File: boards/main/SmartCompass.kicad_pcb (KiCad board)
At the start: 4 copper layers, 70 x 70 mm, 124 parts, among them IC1 Wio-SX1262, J1 SWD HEADER, J2 EXPANSION, J3 FH12A-24S-0.5SH(55), J5 IPEX, P1 JST_BTN_1, P2 JST_BTN_2, P3 JST_BTN_3, Q1 DMG3415U, Q2 Si1308EDL, U1 BMD-340-A-R, U2 MX25R6435FZAIH0, U3 RT9080-33GJ5, U4 MCP73831T-2ACI_OT, U5 MAX17048G_T10, U6 BNO085, U7 DRV2605LDGSR, U8 MAX-M10S-00B, X1 USB4085-GF-A, Y1 32.768KHZ

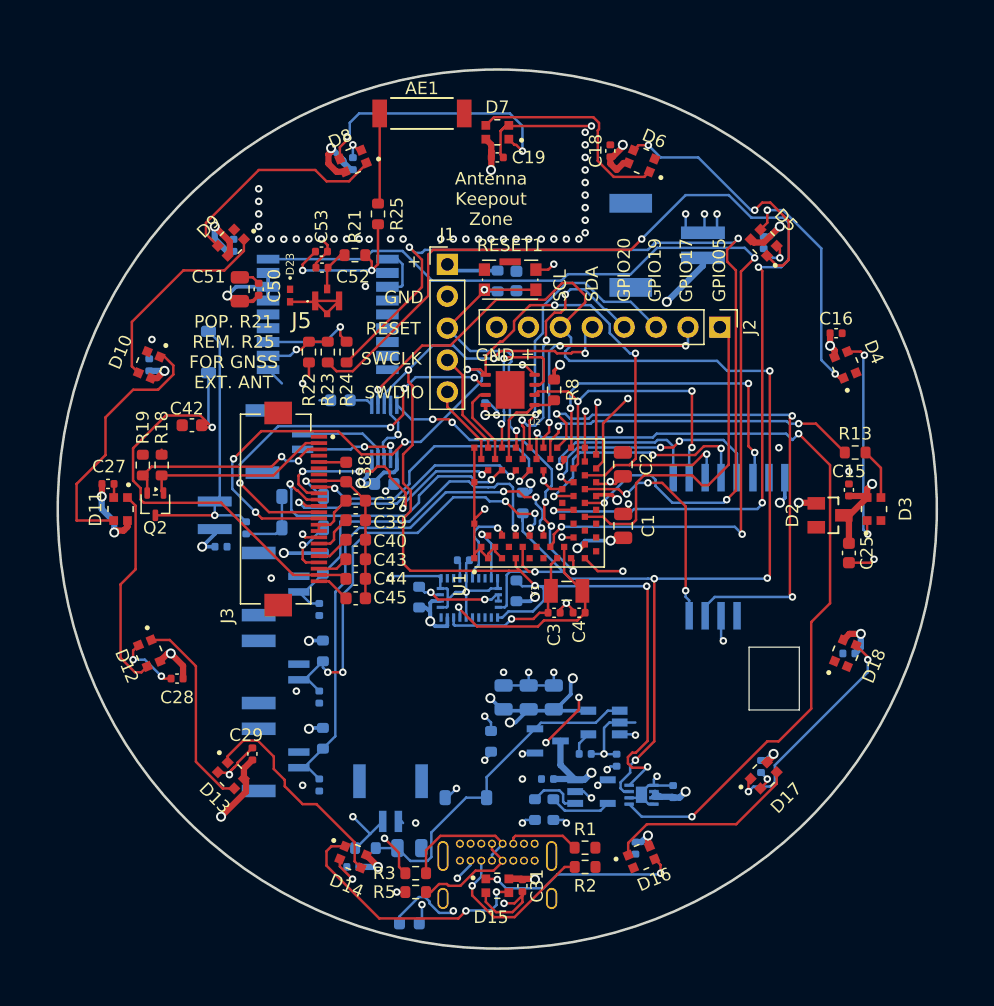
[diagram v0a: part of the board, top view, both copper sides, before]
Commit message: Board migrations. Move to newer LED and IMU
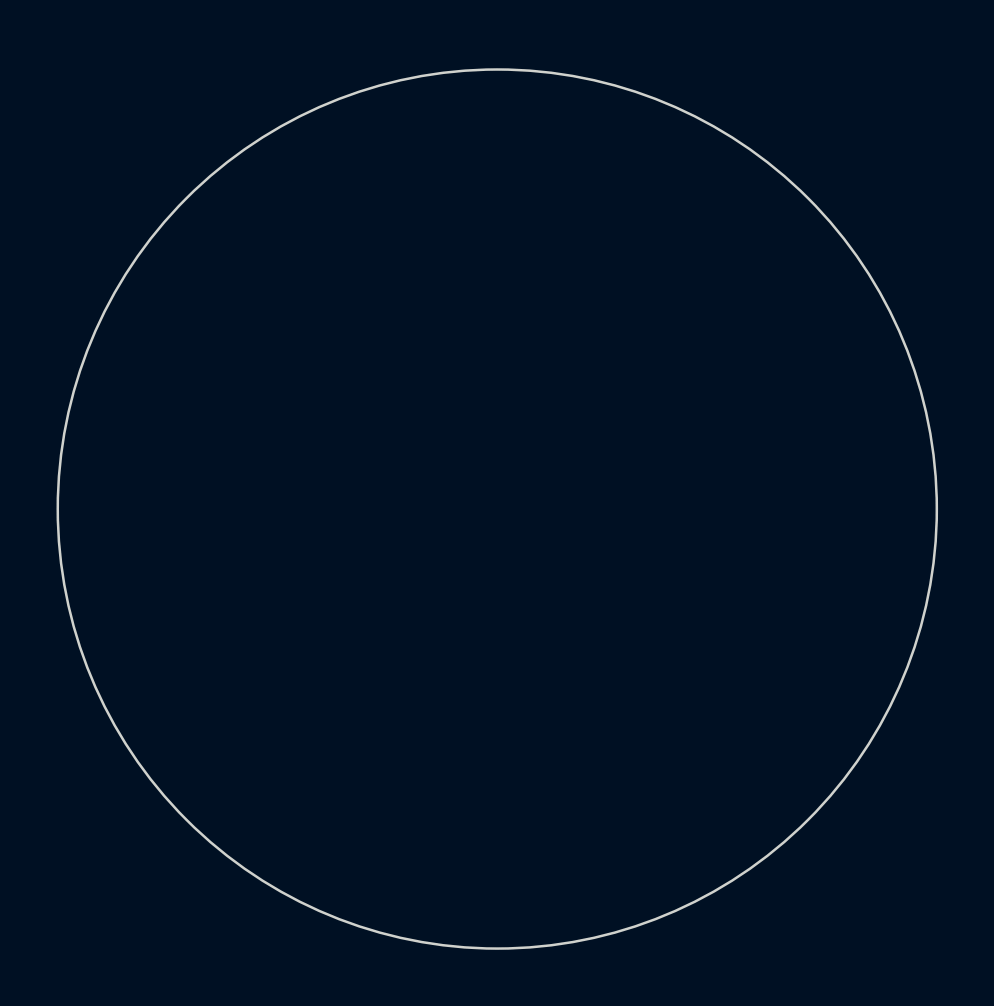
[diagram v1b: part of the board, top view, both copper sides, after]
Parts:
- removed AE1: 1575AT43A0040E, 1575AT43A0040E:ANT_1575AT_JOT
- removed BATT1: JST_PH, S2B-PH-SM4-TB_LF__SN_:JST_S2B-PH-SM4-TB_LF__SN_
- removed C1, C11, C13, C2, C51, C8, C9: 10uF, Capacitor_SMD:C_0805_2012Metric
- removed C10, C14, C15, C16, C17, C18, C19, C20, C21, C22, C23, C24, C26, C27, C28, C29, C30, C31, C32, C33, C34, C35, C50, C6: 0.1uF, Capacitor_SMD:C_0402_1005Metric
- removed C12, C36, C41, C7: 4.7uF, Capacitor_SMD:C_0402_1005Metric
- removed C25: 22uF, Capacitor_SMD:C_0603_1608Metric
- removed C3, C4: 12pF, Capacitor_SMD:C_0402_1005Metric
- removed C37, C38, C39, C40, C42, C43, C44, C45, C46, C47, C5: 1uF, Capacitor_SMD:C_0603_1608Metric
- removed C52, C53: NM, Capacitor_SMD:C_0402_1005Metric
- removed CHG1: ORANGE, LED_SMD:LED_0603_1608Metric
- removed D1, D19, D20, D21: MBR0540, Diode_SMD:D_SOD-123
- removed D10, D11, D12, D13, D14, D15, D16, D17, D18, D3, D4, D5, D6, D7, D8, D9: WS2812B2020, WS2812B2020:LED_WS2812B2020
- removed D2: BAV199, BAV199:SOT23
- removed D23: TPD1E05U06DPYR, TPD1E05U06DPYR:DIO_TPD1E05U06DPYR
- removed HAPTIC1: JST_HAPTIC, SM02B-GHS-TB:JST_SM02B-GHS-TB
- removed IC1: Wio-SX1262, 114993390:114993390
- removed J1: SWD HEADER, Connector_PinHeader_2.54mm:PinHeader_1x05_P2.54mm_Vertical
- removed J2: EXPANSION, Connector_PinHeader_2.54mm:PinHeader_1x08_P2.54mm_Vertical
- removed J3: FH12A-24S-0.5SH(55), FH12-24S-0.5SH_55_:HRS_FH12-24S-0.5SH_55_
- removed J5: IPEX, RECE.20369:RECE20369001E01
- removed L1: 47uH 500mA, Inductor_SMD:L_Taiyo-Yuden_NR-30xx
- removed ONOFF1: JST_ONOFF, SM02B-GHS-TB:JST_SM02B-GHS-TB
- removed P1: JST_BTN_1, SM02B-GHS-TB:JST_SM02B-GHS-TB
- removed P2: JST_BTN_2, SM02B-GHS-TB:JST_SM02B-GHS-TB
- removed P3: JST_BTN_3, SM02B-GHS-TB:JST_SM02B-GHS-TB
- removed Q1: DMG3415U, DMG3415U-7:SOT95P240X105-3N
- removed Q2: Si1308EDL, Package_TO_SOT_SMD:SOT-323_SC-70
- removed R1, R10, R2, R22, R4: 5K, Resistor_SMD:R_0603_1608Metric
- removed R11: 2K, Resistor_SMD:R_0603_1608Metric
- removed R12, R9: 100K, Resistor_SMD:R_0603_1608Metric
- removed R13: 500R, Resistor_SMD:R_0603_1608Metric
- removed R14, R15, R16, R17, R8: 10K, Resistor_SMD:R_0603_1608Metric
- removed R18: 1M, Resistor_SMD:R_0603_1608Metric
- removed R19: 2.2R, Resistor_SMD:R_0603_1608Metric
- removed R21: NM, Resistor_SMD:R_0603_1608Metric
- removed R23, R24: 1K, Resistor_SMD:R_0603_1608Metric
- removed R25: 0R, Resistor_SMD:R_0603_1608Metric
- removed R3, R5: 27R, Resistor_SMD:R_0603_1608Metric
- removed R6, R7: 4.7K, Resistor_SMD:R_0603_1608Metric
- removed RESET1: KMR2, Button_Switch_SMD:SW_Push_1P1T-SH_NO_CK_KMR2xxG
- removed U1: BMD-340-A-R, BMD_340_A_R:RIGADO_BMD-340-A-R
- removed U2: MX25R6435FZAIH0, MX25R6435FZAIH0:SON80P400X400X60-9N
- removed U3: RT9080-33GJ5, RT9080-33GJ5:SOT94P280X100-5N
- removed U4: MCP73831T-2ACI_OT, MCP73831T-2ACI_OT:SOT95P280X145-5N
- removed U5: MAX17048G_T10, MAX17048G_T10:SON50P200X200X80-9N
- removed U6: BNO085, BNO085:IC_BNO085
- removed U7: DRV2605LDGSR, DRV2605LDGSR:SOP50P490X110-10N
- removed U8: MAX-M10S-00B, MAX-M10S-00B:XCVR_MAX-M10S-00B
- removed X1: USB4085-GF-A, USB4085-GF-A:GCT_USB4085-GF-A_REVB
- removed Y1: 32.768KHZ, ABS07-32.768KHZ-7-T:XTAL_ABS07-32.768KHZ-7-T
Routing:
- net GND: track 166.6 -> 0.00 mm, vias 86 -> 0
- net Vdrive: track 116.9 -> 0.00 mm, vias 17 -> 0
- net /SCL: track 113.4 -> 0.00 mm, vias 6 -> 0
- net /TXD_GPS: track 88.7 -> 0.00 mm, vias 4 -> 0
- net /SDA: track 85.2 -> 0.00 mm, vias 6 -> 0
- net /GPS_RESET: track 80.4 -> 0.00 mm, vias 3 -> 0
- net +BATT: track 77.0 -> 0.00 mm, vias 4 -> 0
- net /SPI_MOSI: track 76.6 -> 0.00 mm, vias 7 -> 0
- net +3.3V: track 74.6 -> 0.00 mm, vias 18 -> 0
- net /RXD_GPS: track 74.3 -> 0.00 mm, vias 4 -> 0
- net VBUS: track 70.9 -> 0.00 mm, vias 10 -> 0
- net /SPI_SCK: track 66.5 -> 0.00 mm, vias 7 -> 0
- net /Power and USB/LOW_BATT: track 65.6 -> 0.00 mm, vias 3 -> 0
- net /D-: track 54.5 -> 0.00 mm, vias 2 -> 0
- net /D+: track 50.0 -> 0.00 mm, vias 2 -> 0
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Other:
- outline, holes or cut-outs redrawn
- board text removed: "+"
- board text removed: "3.3V"
- board text removed: "Antenna Keepout Zone"
- board text removed: "CLK"
- board text removed: "DIO"
- board text removed: "GND"
- board text removed: "GPIO05"
- board text removed: "GPIO17"
- board text removed: "GPIO19"
- board text removed: "GPIO20"
- board text removed: "POP. R21 REM. R25 FOR GNSS EXT. ANT"
- board text removed: "RESET"
- board text removed: "RST"
- board text removed: "SCL"
- board text removed: "SDA"
- board text removed: "SWCLK"
- board text removed: "SWDIO"
